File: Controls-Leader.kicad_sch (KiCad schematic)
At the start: 24 parts, among them J24 ExtraGPIO_Conn, J25 UART_TP, J8 SWD, SW10 RESET, U7 STM32F413RHTx, Y1 Crystal

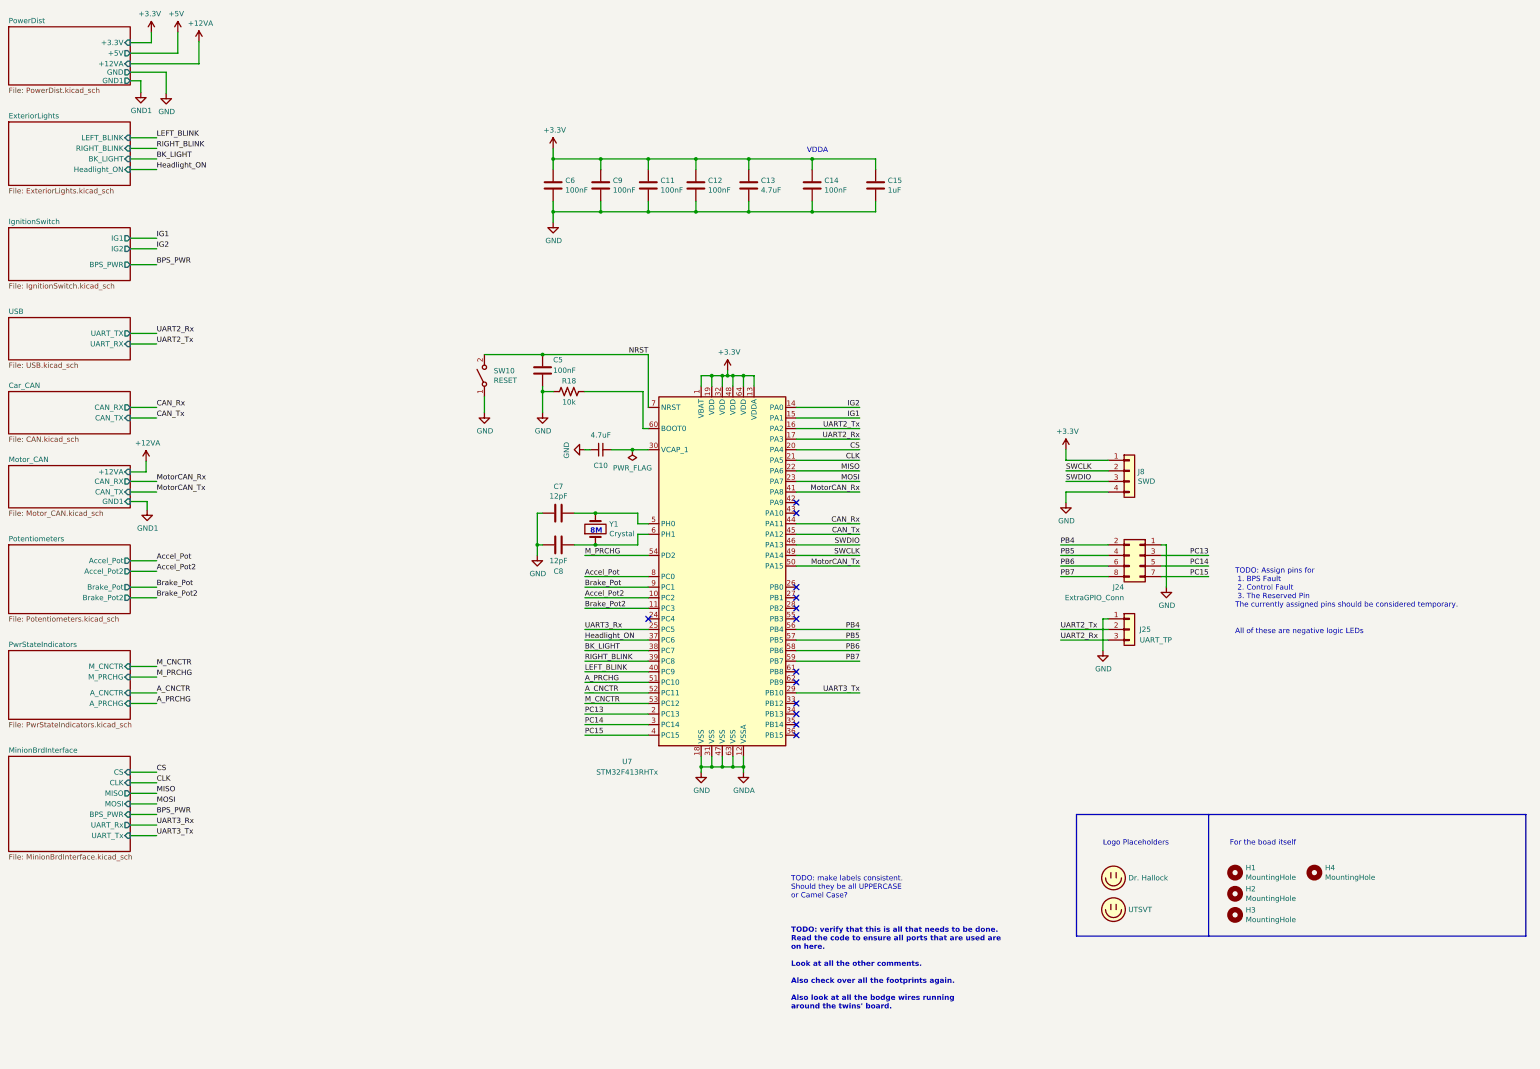
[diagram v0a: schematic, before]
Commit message: Daybreak rework (#24)
* Schematic notations for rework changes

* Updated schematic in accordance to previous weeks annotated changes

* Added .lck files to .gitignore.

* Renamed Clk to PA5, removed CAN_TX/RX test points, deleted other .lck file and #auto_saved_files# (hopefully this does not break anything.

* Changed testpoints to pin headers.

* removed camera, fixed connectors, and changed status LEDS

* Schematic finished :) hopefully not broken

* Added back lights + drivers + timer for all blinkers and brake lights

* Fuse added for motorCAN 12V

* Renamed local net labels to be different from hierarchical ones in the MinionBrdInterface so that they aren't connected. Changed Regen input to BPS Hazard light since we aren't using regen but will be alerting the driver of BPS faults.

* Flipped optoisolators, changed resistor values, added second connector to motor can and disconnected shield pins for now since I haven't seen them used (will chack against old version to see what the circuit looked like), copied power-in circuit from contactor board, added optoisolator to timer and blinker light connection.

* Changed names and added power flags until KiCAD ERC was satisfied. Hopefully this did not involve doing anything that wasn't supposed to be done.

* Added UTSVT libraries to the gitignore.

* Added footprints. I think this is everything except the fuse.

* Fuse footprint added and blinker changed to software

* Started cleaning some comments, changed EL3H7 data sheet link, removed extra motor CAN connector and changed original one to match (I think) motor controller connector, removed extra mounting holes, removed hierarchical power labels.

* renamed power state indicators to contactors and removed unused contactors, added current limiting resistors to lights drivers, changed mosfet to new mosfet

* Updated contactor pins.

* added circuitry for limit switch brake, added mosfet to drive LEDs, cleaned up legacy comments, 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
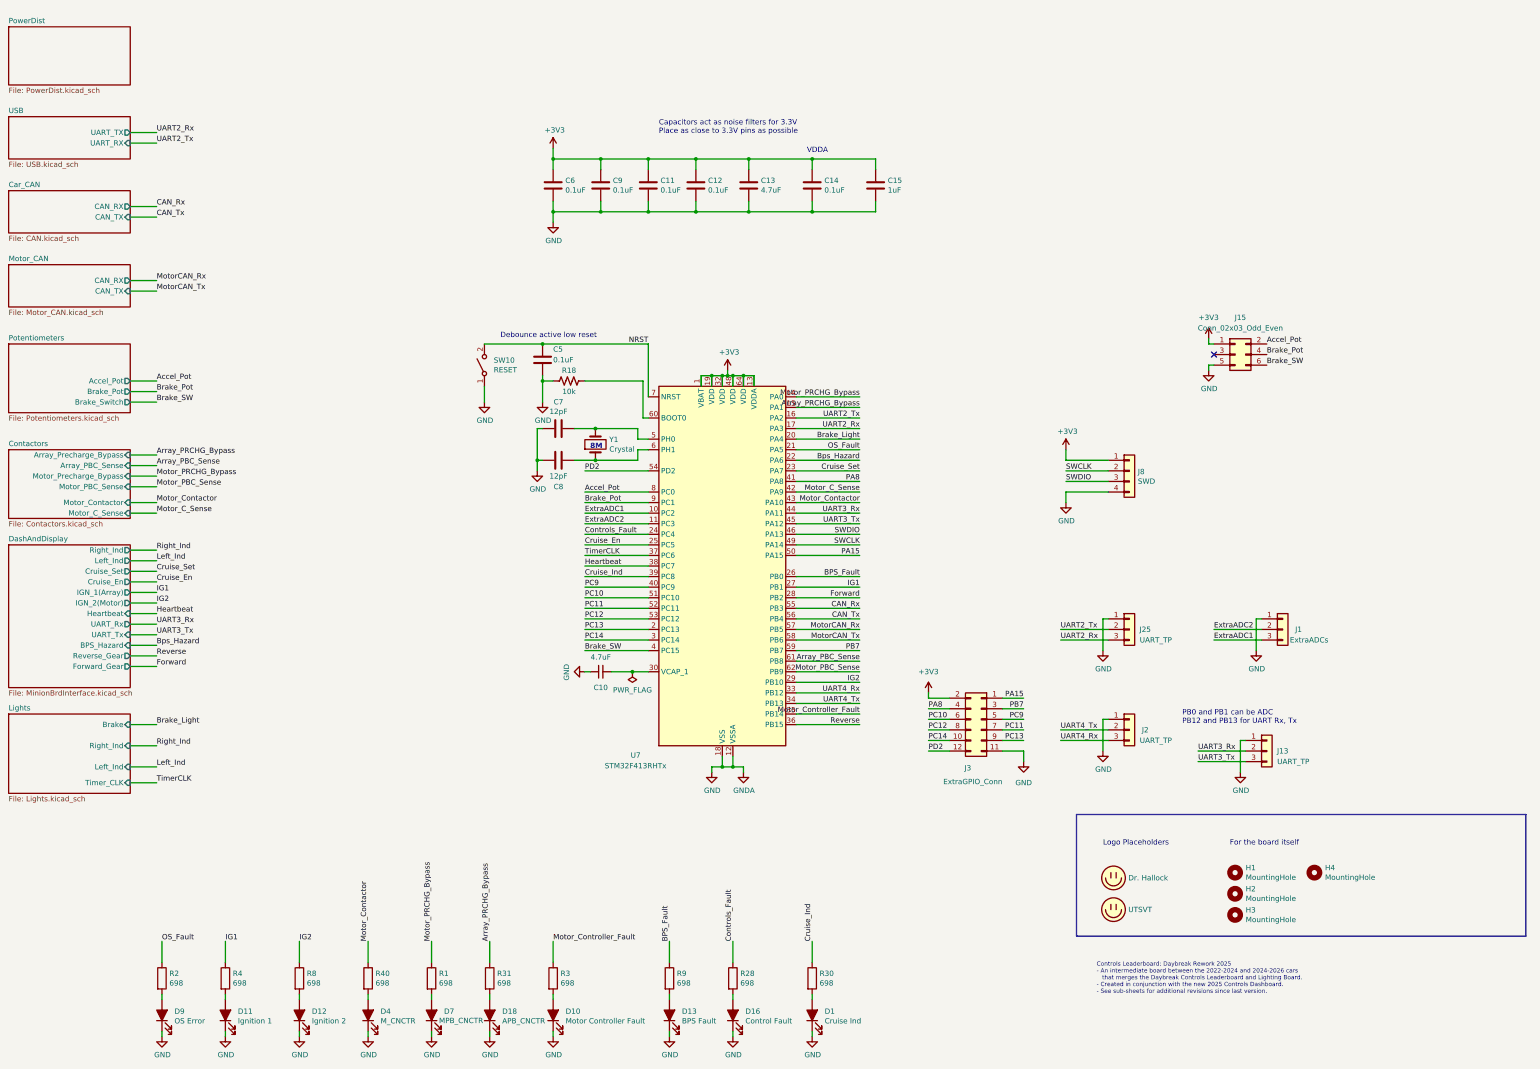
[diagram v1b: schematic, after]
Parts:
- removed J24: ExtraGPIO_Conn, Connector_PinHeader_2.54mm:PinHeader_2x04_P2.54mm_Vertical, symbol Connector_Generic:Conn_02x04_Odd_Even
- added D1: Cruise Ind, LED_SMD:LED_0805_2012Metric, symbol Device:LED_Filled
- added D10: Motor Controller Fault, LED_SMD:LED_0805_2012Metric, symbol Device:LED_Filled
- added D11: Ignition 1, LED_SMD:LED_0805_2012Metric, symbol Device:LED_Filled
- added D12: Ignition 2, LED_SMD:LED_0805_2012Metric, symbol Device:LED_Filled
- added D13: BPS Fault, LED_SMD:LED_0805_2012Metric, symbol Device:LED_Filled
- added D16: Control Fault, LED_SMD:LED_0805_2012Metric, symbol Device:LED_Filled
- added D18: APB_CNCTR, LED_SMD:LED_0805_2012Metric, symbol Device:LED_Filled
- added D4: M_CNCTR, LED_SMD:LED_0805_2012Metric, symbol Device:LED_Filled
- added D7: MPB_CNCTR, LED_SMD:LED_0805_2012Metric, symbol Device:LED_Filled
- added D9: OS Error, LED_SMD:LED_0805_2012Metric, symbol Device:LED_Filled
- added J1: ExtraADCs, UTSVT_Connectors:Molex_MicroFit3.0_1x3xP3.00mm_PolarizingPeg_Vertical, symbol Connector_Generic:Conn_01x03
- added J13, J2: UART_TP, Connector_PinHeader_2.54mm:PinHeader_1x03_P2.54mm_Vertical, symbol Connector_Generic:Conn_01x03
- added J15: Conn_02x03_Odd_Even, Connector_PinHeader_2.54mm:PinHeader_2x03_P2.54mm_Vertical, symbol Connector_Generic:Conn_02x03_Odd_Even
- added J3: ExtraGPIO_Conn, Connector_PinHeader_2.54mm:PinHeader_2x06_P2.54mm_Vertical, symbol Connector_Generic:Conn_02x06_Odd_Even
- added R1, R2, R28, R3, R30, R31, R4, R40, R8, R9: 698, Resistor_SMD:R_0805_2012Metric, symbol Device:R
- C10: Mouser Part Number (none) -> 81-GRM219R6YA475KA3D; P/N (none) -> GRM219R6YA475KA3D
- C11, C12, C14, C5, C6, C9: value 100nF -> 0.1uF; Mouser Part Number 80-C0805C104K3R -> 80-C0805C104M5R; P/N (none) -> C0805C104M5R
- C13: Mouser Part Number 80-C0805C475K3RAUTO -> 81-GRM219R6YA475KA3D; P/N (none) -> GRM219R6YA475KA3D
- C15: Mouser Part Number 80-C0805C104K3R -> (none); P/N (none) -> C0805C105J3RECAUTO
- C7, C8: Mouser Part Number 80-C0805C479K1G -> 80-C0805C120K5HACTU; P/N (none) -> C0805C120K5HACTU
- LOGO1, LOGO2: symbol Dashboard-rescue:Logo_Placeholder-utsvt-misc -> utsvt-misc:Logo_Placeholder
- R18: P/N (none) -> CRCW080510K0FKEAC
- SW10: P/N (none) -> B3SL-1002P
- U7: Mouser Part Number (none) -> 511-STM32F413RHT6; P/N (none) -> STM32F413RHT6
- Y1: P/N (none) -> ABM3-8.000MHZ-D2Y-T
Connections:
- net PB4 is gone; now on net CAN_Tx: U7.56 (PB4)
- net PB5 is gone; now on net MotorCAN_Rx: U7.57 (PB5)
- net PB6 is gone; now on net MotorCAN_Tx: U7.58 (PB6)
- net +3V3: now also J15.1 (Pin_1), J3.2 (Pin_2)
- net Accel_Pot: now also J15.2 (Pin_2)
- net Brake_Pot: now also J15.4 (Pin_4)
- net CAN_Rx: now also U7.55 (PB3); no longer U7.44 (PA11)
- net CAN_Tx: no longer U7.45 (PA12)
- net GND: now also D1.1 (K), D10.1 (K), D11.1 (K), D12.1 (K), D13.1 (K), D16.1 (K), D18.1 (K), D4.1 (K), D7.1 (K), D9.1 (K), J1.1 (Pin_1), J13.1 (Pin_1), J15.5 (Pin_5), J2.1 (Pin_1), J3.11 (Pin_11)
- net IG1: now also U7.27 (PB1), R4.1; no longer U7.15 (PA1)
- net IG2: now also U7.29 (PB10), R8.1; no longer U7.14 (PA0)
- net MotorCAN_Rx: no longer U7.41 (PA8)
- net MotorCAN_Tx: no longer U7.50 (PA15)
- net PB7: now also J3.3 (Pin_3)
- net PC13: now also J3.9 (Pin_9)
- net PC14: now also J3.10 (Pin_10)
- net UART3_Rx: now also U7.44 (PA11), J13.2 (Pin_2); no longer U7.25 (PC5)
- net UART3_Tx: now also U7.45 (PA12), J13.3 (Pin_3); no longer U7.29 (PB10)
- net Controls_Fault: now reaches U7.24 (PC4)
- net Controls_Fault: now also R28.1
- net BPS_Fault: now reaches U7.26 (PB0)
- net BPS_Fault: now also R9.1
- net Forward: now reaches U7.28 (PB2)
- net UART4_Rx: now reaches U7.33 (PB12)
- net UART4_Rx: now also J2.3 (Pin_3)
- net UART4_Tx: now reaches U7.34 (PB13)
- net UART4_Tx: now also J2.2 (Pin_2)
- net Motor_Controller_Fault: now reaches U7.35 (PB14)
- net Motor_Controller_Fault: now also R3.1
- net Reverse: now reaches U7.36 (PB15)
- net Motor_C_Sense: now reaches U7.42 (PA9)
- net Motor_Contactor: now reaches U7.43 (PA10)
- net Motor_Contactor: now also R40.1
- net Array_PBC_Sense: now reaches U7.61 (PB8)
- net Motor_PBC_Sense: now reaches U7.62 (PB9)
- net A_CNCTR renamed PC11
- net PC11: now also J3.7 (Pin_7)
- net A_PRCHG renamed PC10
- net PC10: now also J3.6 (Pin_6)
- net Accel_Pot2 renamed ExtraADC1
- net ExtraADC1: now also J1.3 (Pin_3)
- net BK_LIGHT renamed Heartbeat
- net Brake_Pot2 renamed ExtraADC2
- net ExtraADC2: now also J1.2 (Pin_2)
- net CLK renamed OS_Fault
- net OS_Fault: now also R2.1
- net CS renamed Brake_Light
- net Headlight_ON renamed TimerCLK
- net LEFT_BLINK renamed PC9
- net PC9: now also J3.5 (Pin_5)
- net MISO renamed Bps_Hazard
- net MOSI renamed Cruise_Set
- net M_CNCTR renamed PC12
- net PC12: now also J3.8 (Pin_8)
- net M_PRCHG renamed PD2
- net PD2: now also J3.12 (Pin_12)
- net PC15 renamed Brake_SW
- net Brake_SW: now also J15.6 (Pin_6)
- net RIGHT_BLINK renamed Cruise_Ind
- net Cruise_Ind: now also R30.1
- new net: D11.2 (A), R4.2
- new net: D16.2 (A), R28.2
- new net: D1.2 (A), R30.2
- new net: D4.2 (A), R40.2
- new net: D9.2 (A), R2.2
- new net: D13.2 (A), R9.2
- new net: D10.2 (A), R3.2
- new net: D18.2 (A), R31.2
- new net: D7.2 (A), R1.2
- new net: D12.2 (A), R8.2
- new net Array_PRCHG_Bypass: R31.1, U7.15 (PA1)
- new net Cruise_En: U7.25 (PC5)
- new net Motor_PRCHG_Bypass: R1.1, U7.14 (PA0)
- new net PA15: J3.1 (Pin_1), U7.50 (PA15)
- new net PA8: J3.4 (Pin_4), U7.41 (PA8)
- no-connect marks 13 -> 1
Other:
- sheet MinionBrdInterface renamed DashAndDisplay
- sheet PwrStateIndicators renamed Contactors
- removed sheet ExteriorLights
- removed sheet IgnitionSwitch
- added sheet Lights (Lights.kicad_sch)
- sheet Contactors: file PwrStateIndicators.kicad_sch -> Contactors.kicad_sch
- sheet Contactors ports: added Array_PBC_Sense, Array_Precharge_Bypass, Motor_C_Sense, Motor_Contactor, Motor_PBC_Sense, Motor_Precharge_Bypass; removed A_CNCTR, A_PRCHG, M_CNCTR, M_PRCHG
- sheet DashAndDisplay ports: added BPS_Hazard, Cruise_En, Cruise_Set, Forward_Gear, Heartbeat, IGN_1(Array), IGN_2(Motor), Left_Ind, Reverse_Gear, Right_Ind; removed BPS_PWR, CLK, CS, MISO, MOSI
- sheet Motor_CAN ports: added none; removed +12VA, GND1
- sheet Potentiometers ports: added Brake_Switch; removed Accel_Pot2, Brake_Pot2
- sheet PowerDist ports: added none; removed +12VA, +3.3V, +5V, GND, GND1
- note added: "Capacitors act as noise filters for 3.3V Place as close to 3.3V pins as possible"
- note added: "Controls Leaderboard: Daybreak Rework 2025 - An intermediate board between the 2022-2024 and 2024-2026 cars that merges the Daybreak Controls Leaderboard and Lighting Board. - Created in conjunction with the new 2025 Controls Dashboard. - See sub-sheets for additional revisions since last version."
- note added: "Debounce active low reset"
- note added: "For the board itself"
- note added: "PB0 and PB1 can be ADC PB12 and PB13 for UART Rx, Tx"
- note removed: "All of these are negative logic LEDs"
- note removed: "For the boad itself"
- note removed: "TODO: Assign pins for 1. BPS Fault 2. Control Fault 3. The Reserved Pin The currently assigned pins should be considered temporary."
- note removed: "TODO: make labels consistent. Should they be all UPPERCASE or Camel Case?"
- note removed: "TODO: verify that this is all that needs to be done. Read the code to ensure all ports that are used are on here. Look at all the other comments. Also check over all the footprints again. Also look at all the bodge wires running around the twins' board."
- company: UTSVT -> LHRS
- title: Dashboard -> Controls Leader
- moved on the sheet: C10, C5, C7, C8, R18, SW10, Y1

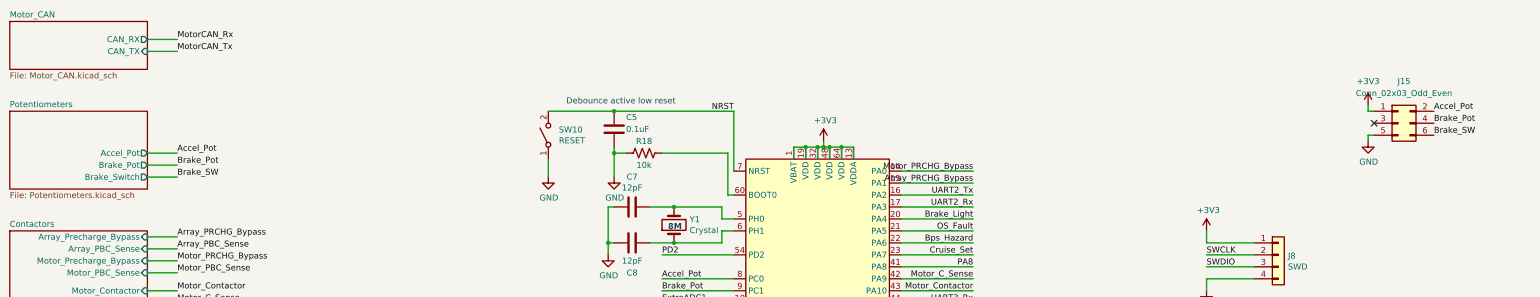
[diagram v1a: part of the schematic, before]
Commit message: Added resistor divider to support 5V potentiometer
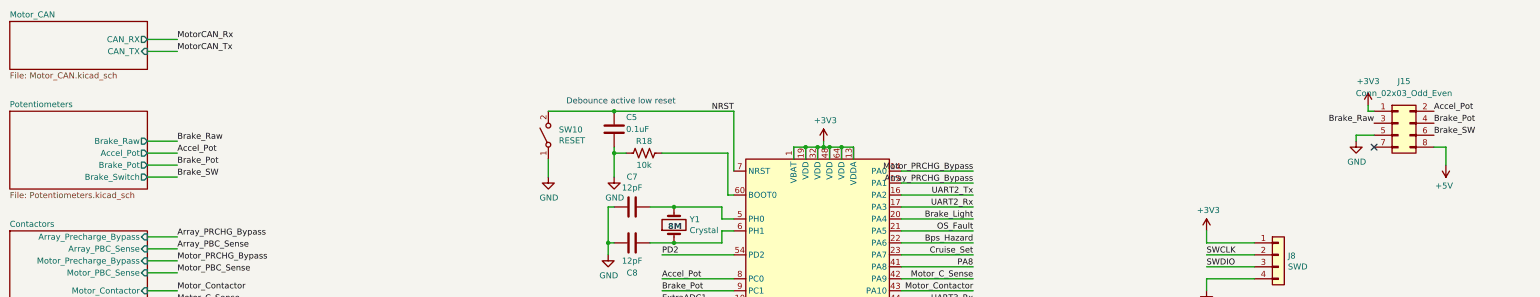
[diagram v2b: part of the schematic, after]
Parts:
- J15: footprint Connector_PinHeader_2.54mm:PinHeader_2x03_P2.54mm_Vertical -> Connector_PinHeader_2.54mm:PinHeader_2x04_P2.54mm_Vertical; symbol Connector_Generic:Conn_02x03_Odd_Even -> Connector_Generic:Conn_02x04_Odd_Even
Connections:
- net Brake_Raw: now reaches J15.3 (Pin_3)
- new net +5V: J15.8 (Pin_8)
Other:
- sheet Potentiometers ports: added Brake_Raw; removed none
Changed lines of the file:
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@@
 	)
 	(no_connect
-		(at 328.93 107.95)
+		(at 328.93 113.03)
 	)
 	(wire
@@
 	(wire
 		(pts
-			(xy 327.66 111.76) (xy 327.66 110.49)
+			(xy 325.12 111.76) (xy 325.12 110.49)
 		)
 		(stroke
@@
 	(wire
 		(pts
+			(xy 341.63 113.03) (xy 344.17 113.03)
+		)
+		(stroke
+			(width 0)
+			(type default)
+		)
+	)
+	(wire
+		(pts
 			(xy 190.5 130.81) (xy 190.5 133.35)
 		)
@@
 		)
 	)
+	(wire
+		(pts
+			(xy 344.17 113.03) (xy 344.17 116.84)
+		)
+		(stroke
+			(width 0)
+			(type default)
+		)
+	)
 	(polyline
 		(pts
@@
 	(wire
 		(pts
+			(xy 68.58 111.76) (xy 74.93 111.76)
+		)
+		(stroke
+			(width 0)
+			(type default)
+		)
+	)
+	(wire
+		(pts
 			(xy 177.8 166.37) (xy 193.04 166.37)
 		)
@@
 	(wire
 		(pts
-			(xy 327.66 110.49) (xy 328.93 110.49)
+			(xy 325.12 110.49) (xy 328.93 110.49)
 		)
 		(stroke
@@
 		)
 	)
+	(label "Brake_Raw"
+		(at 74.93 111.76 0)
+		(fields_autoplaced yes)
+		(effects
+			(font
+				(size 1.27 1.27)
+			)
+			(justify left bottom)
+		)
+	)
 	(label "UART3_Tx"
 		(at 243.84 148.59 180)
@@
 		)
 	)
+	(label "Brake_Raw"
+		(at 328.93 107.95 180)
+		(fields_autoplaced yes)
+		(effects
+			(font
+				(size 1.27 1.27)
+			)
+			(justify right bottom)
+		)
+	)
 	(label "UART2_Tx"
 		(at 74.93 57.15 0)
@@
 	)
 	(symbol
+		(lib_id "power:+5V")
+		(at 344.17 116.84 180)
+		(unit 1)
+		(exclude_from_sim no)
+		(in_bom yes)
+		(on_board yes)
+		(dnp no)
+		(property "Reference" "#PWR0113"
+			(at 344.17 113.03 0)
+			(effects
+				(font
+					(size 1.27 1.27)
+				)
+				(hide yes)
+			)
+		)
+		(property "Value" "+5V"
+			(at 343.789 121.2342 0)
+			(effects
+				(font
+					(size 1.27 1.27)
+				)
+			)
+		)
+		(property "Footprint" ""
+			(at 344.17 116.84 0)
+			(effects
+				(font
+					(size 1.27 1.27)
+				)
+				(hide yes)
+			)
+		)
+		(property "Datasheet" ""
+			(at 344.17 116.84 0)
+			(effects
+				(font
+					(size 1.27 1.27)
+				)
+				(hide yes)
+			)
+		)
+		(property "Description" "Power symbol creates a global label with name \"+5V\""
+			(at 344.17 116.84 0)
+			(effects
+				(font
+					(size 1.27 1.27)
+				)
+				(hide yes)
+			)
+		)
+		(pin "1"
+		)
+		(instances
+			(project "Controls-Leader"
+				(path "/66218487-e316-4467-9eba-79d4626ab24e"
+					(reference "#PWR0113")
+					(unit 1)
+				)
+			)
+		)
+	)
+	(symbol
 		(lib_id "Device:R")
 		(at 232.41 257.81 0)
@@
 	)
 	(symbol
-		(lib_id "Connector_Generic:Conn_02x03_Odd_Even")
+		(lib_id "Connector_Generic:Conn_02x04_Odd_Even")
 		(at 334.01 107.95 0)
 		(unit 1)
@@
 			)
 		)
-		(property "Footprint" "Connector_PinHeader_2.54mm:PinHeader_2x03_P2.54mm_Vertical"
+		(property "Footprint" "Connector_PinHeader_2.54mm:PinHeader_2x04_P2.54mm_Vertical"
 			(at 334.01 107.95 0)
 			(effects
@@
 			)
 		)
-		(property "Description" "Generic connector, double row, 02x03, odd/even pin numbering scheme (row 1 odd numbers, row 2 even numbers), script generated (kicad-library-utils/schlib/autogen/connector/)"
+		(property "Description" "Generic connector, double row, 02x04, odd/even pin numbering scheme (row 1 odd numbers, row 2 even numbers), script generated (kicad-library-utils/schlib/autogen/connector/)"
 			(at 334.01 107.95 0)
 			(effects
@@
 		(pin "4"
 		)
+		(pin "8"
+		)
+		(pin "7"
+		)
 		(instances
 			(project ""
@@
 	(symbol
 		(lib_id "power:GND")
-		(at 327.66 111.76 0)
+		(at 325.12 111.76 0)
 		(unit 1)
 		(exclude_from_sim no)
@@
 		(dnp no)
 		(property "Reference" "#PWR034"
-			(at 327.66 118.11 0)
+			(at 325.12 118.11 0)
 			(effects
 				(font
@@
 		)
 		(property "Value" "GND"
-			(at 327.787 116.1542 0)
+			(at 325.247 116.1542 0)
 			(effects
 				(font
@@
 		)
 		(property "Footprint" ""
-			(at 327.66 111.76 0)
+			(at 325.12 111.76 0)
 			(effects
 				(font
@@
 		)
 		(property "Datasheet" ""
-			(at 327.66 111.76 0)
+			(at 325.12 111.76 0)
 			(effects
 				(font
@@
 		)
 		(property "Description" "Power symbol creates a global label with name \"GND\" , ground"
-			(at 327.66 111.76 0)
+			(at 325.12 111.76 0)
 			(effects
 				(font
@@
 			(effects
 				(font
+					(size 1.27 1.27)
+				)
+				(justify right)
+			)
+		)
+		(pin "Brake_Raw" output
+			(at 68.58 111.76 0)
+			(effects
+				(font
